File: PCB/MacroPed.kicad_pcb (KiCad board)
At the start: 2 copper layers, 82.4 x 52.1 mm, 11 parts, among them J1 Conn_01x02_Socket, J2 Conn_01x02_Socket, J3 Conn_01x02_Socket, J4 Conn_01x02_Socket, J5 Conn_01x02_Socket, J6 Conn_01x02_Socket, J7 Conn_01x02_Socket, J8 Conn_01x02_Socket, J9 Conn_01x02_Socket, SW1 SW_SPST, U1 Pico

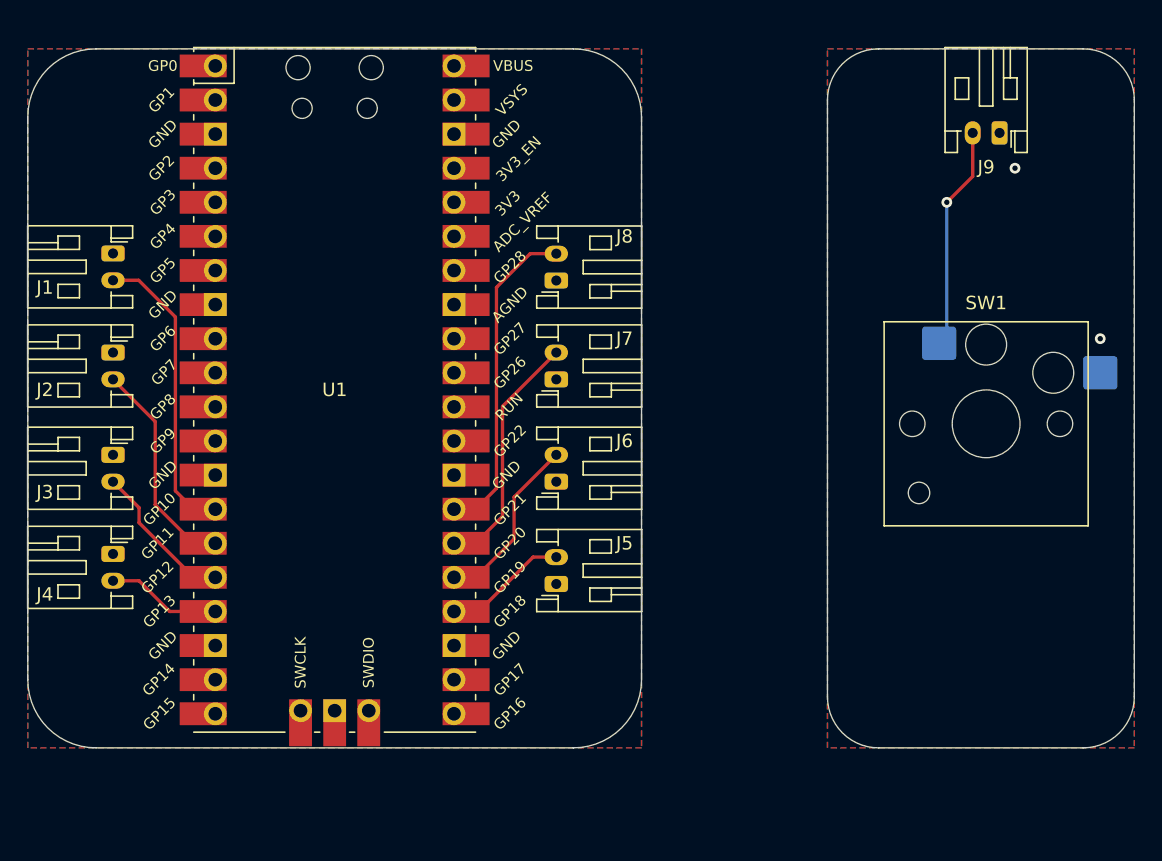
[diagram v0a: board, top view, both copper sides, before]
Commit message: Separated daughterboard to sub-project, added mounting holes
Signed-off-by: Devnol <pgkoutsoumanis@gmail.com>
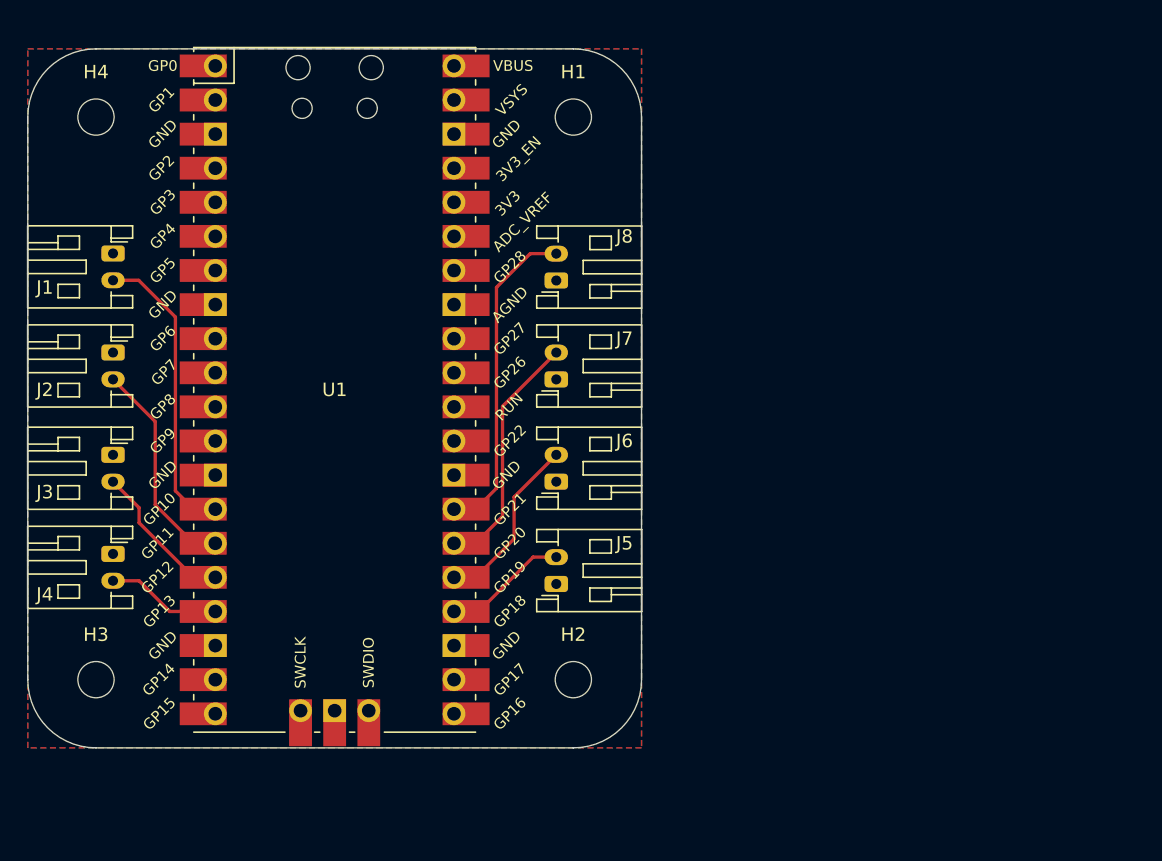
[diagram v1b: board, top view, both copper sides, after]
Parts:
- removed J9: Conn_01x02_Socket, Connector_JST:JST_PH_S2B-PH-K_1x02_P2.00mm_Horizontal
- removed SW1: SW_SPST, PCM_Switch_Keyboard_Hotswap_Kailh:SW_Hotswap_Kailh_Choc_V1V2_2.00u_90deg
- added H1: MountingHole, MountingHole:MountingHole_2.7mm_M2.5_DIN965, F.Cu at (82.5, 26.7)
- added H2: MountingHole, MountingHole:MountingHole_2.7mm_M2.5_DIN965, F.Cu at (82.5, 68.6)
- added H3: MountingHole, MountingHole:MountingHole_2.7mm_M2.5_DIN965, F.Cu at (47.0, 68.6)
- added H4: MountingHole, MountingHole:MountingHole_2.7mm_M2.5_DIN965, F.Cu at (47.0, 26.7)
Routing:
- net Net-(J9-Pin_2): track 16.7 -> 0.00 mm, vias 1 -> 0
- net /Foot Switch/GND: vias 2 -> 0
- removed copper zone on B.Cu, net /Foot Switch/GND
- removed copper zone on F.Cu, net /Foot Switch/GND
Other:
- board size 82.4 x 52.1 mm -> 45.7 x 52.1 mm

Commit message: Move connectors to one side, change dimensions to proper units
Signed-off-by: Devnol <pgkoutsoumanis@gmail.com>
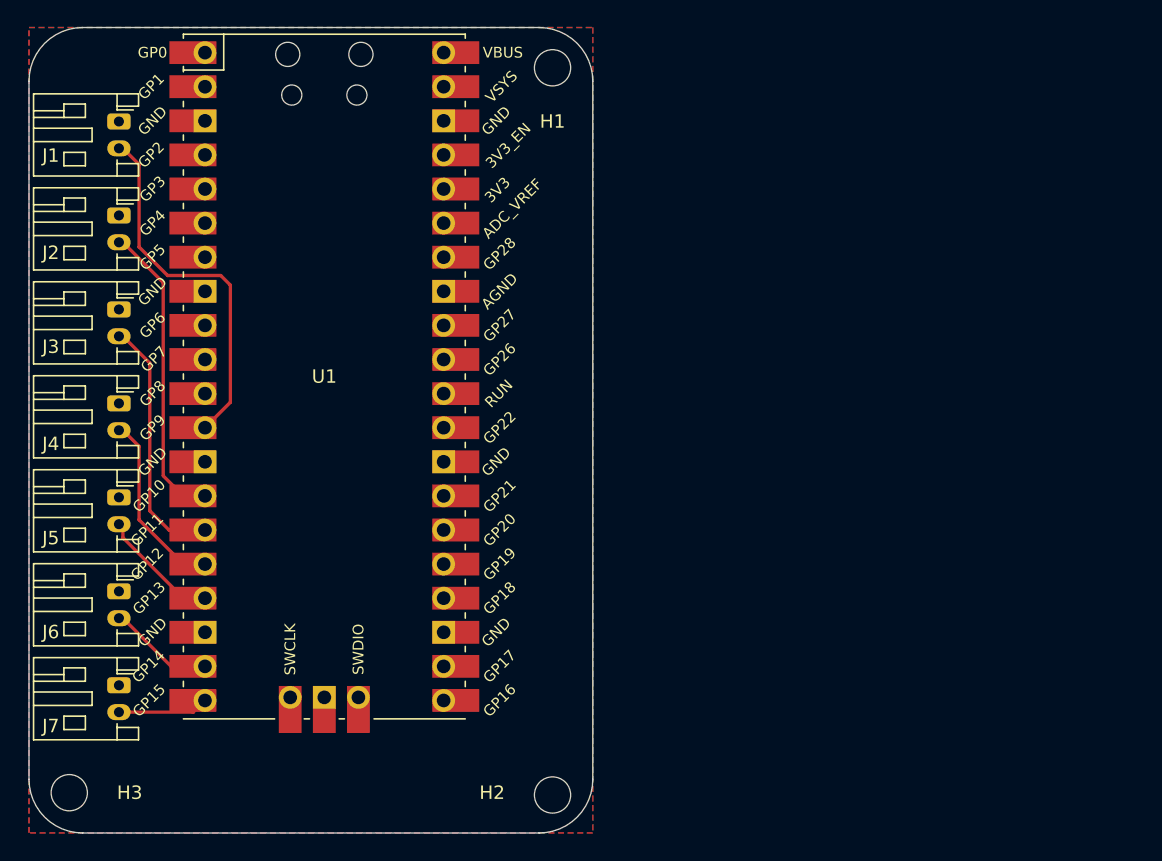
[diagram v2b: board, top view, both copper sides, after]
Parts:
- removed H4: MountingHole, MountingHole:MountingHole_2.7mm_M2.5_DIN965
- removed J8: Conn_01x02_Socket, Connector_JST:JST_PH_S2B-PH-K_1x02_P2.00mm_Horizontal
- moved J7 39.8 mm to (48.7, 69.0), turned to -90 degrees
- moved J6 33.6 mm to (48.7, 62.0), turned to -90 degrees
- moved J5 33.2 mm to (48.7, 55.0), turned to -90 degrees
- moved J4 11.2 mm to (48.7, 48.0)
- moved J3 10.8 mm to (48.7, 41.0)
- moved J2 10.2 mm to (48.7, 34.0)
- moved J1 9.84 mm to (48.7, 27.0)
- moved H2 8.73 mm to (81.0, 77.2)
- moved H3 8.65 mm to (45.0, 77.0)
- moved H1 3.98 mm to (81.0, 23.0)
- moved U1 1.25 mm to (64.0, 46.0)
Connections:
- U1 pad 12: unconnected-(U1-GPIO9-Pad12) -> Net-(J1-Pin_2)
- U1 pad 14: Net-(J1-Pin_2) -> Net-(J2-Pin_2)
- U1 pad 15: Net-(J2-Pin_2) -> Net-(J3-Pin_2)
- U1 pad 16: Net-(J3-Pin_2) -> Net-(J4-Pin_2)
- U1 pad 17: Net-(J4-Pin_2) -> Net-(J5-Pin_2)
- U1 pad 19: unconnected-(U1-GPIO14-Pad19) -> Net-(J6-Pin_2)
- U1 pad 20: unconnected-(U1-GPIO15-Pad20) -> Net-(J7-Pin_2)
- U1 pad 24: Net-(J5-Pin_2) -> unconnected-(U1-GPIO18-Pad24)
- U1 pad 25: Net-(J6-Pin_2) -> unconnected-(U1-GPIO19-Pad25)
- U1 pad 26: Net-(J7-Pin_2) -> unconnected-(U1-GPIO20-Pad26)
- U1 pad 27: Net-(J8-Pin_2) -> unconnected-(U1-GPIO21-Pad27)
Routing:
- net Net-(J8-Pin_2): track 24.3 -> 0.00 mm
- net Net-(J7-Pin_2): track 18.3 -> 6.47 mm
- net Net-(J3-Pin_2): track 11.2 -> 18.5 mm
- net Net-(J2-Pin_2): track 16.3 -> 22.4 mm
- net Net-(J6-Pin_2): track 13.2 -> 7.60 mm
- net Net-(J1-Pin_2): track 22.3 -> 27.2 mm
- net Net-(J4-Pin_2): track 8.57 -> 13.4 mm
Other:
- board size 45.7 x 52.1 mm -> 42 x 60 mm

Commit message: Change board dimensions to real units
Signed-off-by: Devnol <pgkoutsoumanis@gmail.com>
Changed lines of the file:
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@@
     (fp_line (start 3.95 6.25) (end 3.95 -1.35)
       (stroke (width 0.1) (type solid)) (layer "F.Fab"))
-    (pad "1" thru_hole roundrect (at 0 0 270) (size 1.2 1.75) (drill 0.75) (layers "*.Cu" "*.Mask") (roundrect_rratio 0.208333)
+    (pad "1" thru_hole roundrect (at 0 0 270) (size 1.2 1.75) (drill 0.75) (layers "*.Cu" "*.Mask") (roundrect_rratio 0.2083333333)
       (net 10 "/GND") (pinfunction "Pin_1") (pintype "passive"))
     (pad "2" thru_hole oval (at 2 0 270) (size 1.2 1.75) (drill 0.75) (layers "*.Cu" "*.Mask")
@@
     (fp_line (start 3.95 6.25) (end 3.95 -1.35)
       (stroke (width 0.1) (type solid)) (layer "F.Fab"))
-    (pad "1" thru_hole roundrect (at 0 0 270) (size 1.2 1.75) (drill 0.75) (layers "*.Cu" "*.Mask") (roundrect_rratio 0.208333)
+    (pad "1" thru_hole roundrect (at 0 0 270) (size 1.2 1.75) (drill 0.75) (layers "*.Cu" "*.Mask") (roundrect_rratio 0.2083333333)
       (net 10 "/GND") (pinfunction "Pin_1") (pintype "passive"))
     (pad "2" thru_hole oval (at 2 0 270) (size 1.2 1.75) (drill 0.75) (layers "*.Cu" "*.Mask")
@@
     (fp_line (start 3.95 6.25) (end 3.95 -1.35)
       (stroke (width 0.1) (type solid)) (layer "F.Fab"))
-    (pad "1" thru_hole roundrect (at 0 0 270) (size 1.2 1.75) (drill 0.75) (layers "*.Cu" "*.Mask") (roundrect_rratio 0.208333)
+    (pad "1" thru_hole roundrect (at 0 0 270) (size 1.2 1.75) (drill 0.75) (layers "*.Cu" "*.Mask") (roundrect_rratio 0.2083333333)
       (net 10 "/GND") (pinfunction "Pin_1") (pintype "passive"))
     (pad "2" thru_hole oval (at 2 0 270) (size 1.2 1.75) (drill 0.75) (layers "*.Cu" "*.Mask")
@@
     (fp_line (start 3.95 6.25) (end 3.95 -1.35)
       (stroke (width 0.1) (type solid)) (layer "F.Fab"))
-    (pad "1" thru_hole roundrect (at 0 0 270) (size 1.2 1.75) (drill 0.75) (layers "*.Cu" "*.Mask") (roundrect_rratio 0.208333)
+    (pad "1" thru_hole roundrect (at 0 0 270) (size 1.2 1.75) (drill 0.75) (layers "*.Cu" "*.Mask") (roundrect_rratio 0.2083333333)
       (net 10 "/GND") (pinfunction "Pin_1") (pintype "passive"))
     (pad "2" thru_hole oval (at 2 0 270) (size 1.2 1.75) (drill 0.75) (layers "*.Cu" "*.Mask")
@@
     (fp_line (start 3.95 6.25) (end 3.95 -1.35)
       (stroke (width 0.1) (type solid)) (layer "F.Fab"))
-    (pad "1" thru_hole roundrect (at 0 0 270) (size 1.2 1.75) (drill 0.75) (layers "*.Cu" "*.Mask") (roundrect_rratio 0.208333)
+    (pad "1" thru_hole roundrect (at 0 0 270) (size 1.2 1.75) (drill 0.75) (layers "*.Cu" "*.Mask") (roundrect_rratio 0.2083333333)
       (net 10 "/GND") (pinfunction "Pin_1") (pintype "passive"))
     (pad "2" thru_hole oval (at 2 0 270) (size 1.2 1.75) (drill 0.75) (layers "*.Cu" "*.Mask")
@@
     (fp_line (start 3.95 6.25) (end 3.95 -1.35)
       (stroke (width 0.1) (type solid)) (layer "F.Fab"))
-    (pad "1" thru_hole roundrect (at 0 0 270) (size 1.2 1.75) (drill 0.75) (layers "*.Cu" "*.Mask") (roundrect_rratio 0.208333)
+    (pad "1" thru_hole roundrect (at 0 0 270) (size 1.2 1.75) (drill 0.75) (layers "*.Cu" "*.Mask") (roundrect_rratio 0.2083333333)
       (net 10 "/GND") (pinfunction "Pin_1") (pintype "passive"))
     (pad "2" thru_hole oval (at 2 0 270) (size 1.2 1.75) (drill 0.75) (layers "*.Cu" "*.Mask")
@@
     (fp_line (start 3.95 6.25) (end 3.95 -1.35)
       (stroke (width 0.1) (type solid)) (layer "F.Fab"))
-    (pad "1" thru_hole roundrect (at 0 0 270) (size 1.2 1.75) (drill 0.75) (layers "*.Cu" "*.Mask") (roundrect_rratio 0.208333)
+    (pad "1" thru_hole roundrect (at 0 0 270) (size 1.2 1.75) (drill 0.75) (layers "*.Cu" "*.Mask") (roundrect_rratio 0.2083333333)
       (net 10 "/GND") (pinfunction "Pin_1") (pintype "passive"))
     (pad "2" thru_hole oval (at 2 0 270) (size 1.2 1.75) (drill 0.75) (layers "*.Cu" "*.Mask")

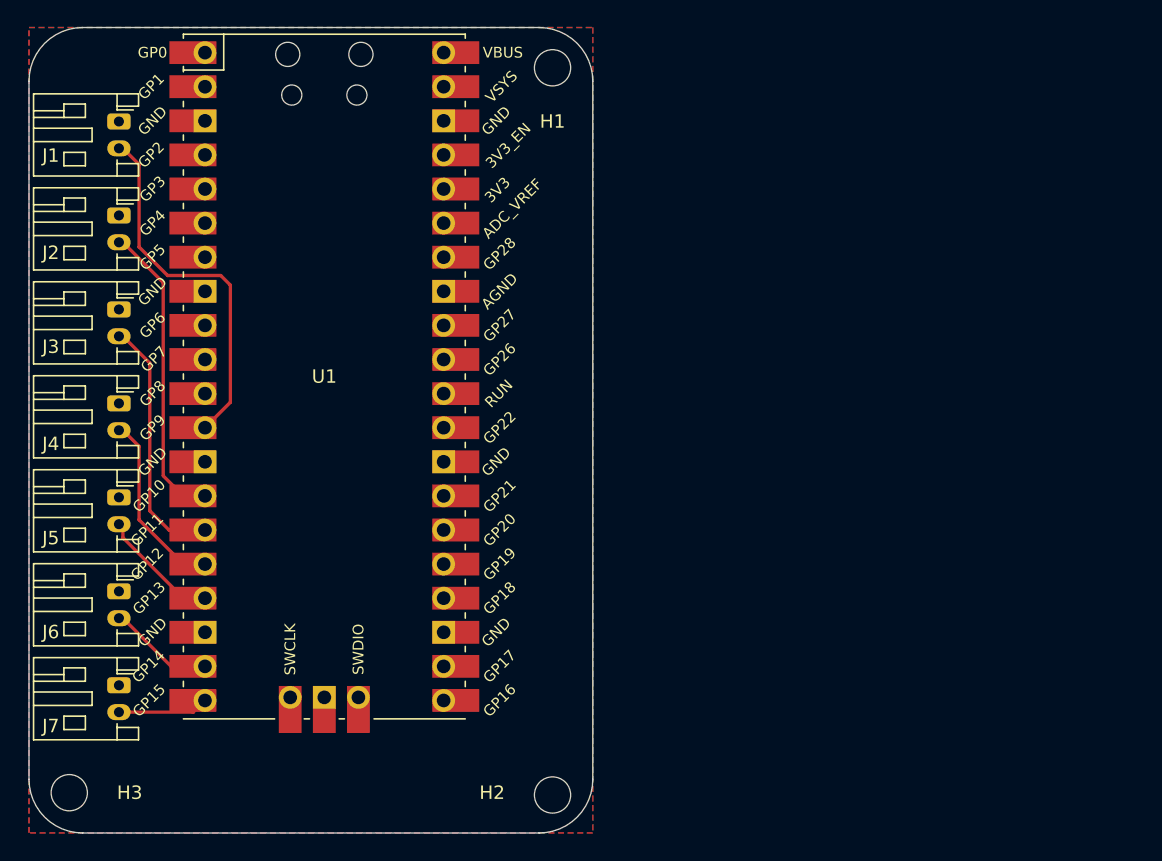
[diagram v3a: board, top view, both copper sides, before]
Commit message: Moved JST connector to edge of footboard
Signed-off-by: Devnol <pgkoutsoumanis@gmail.com>
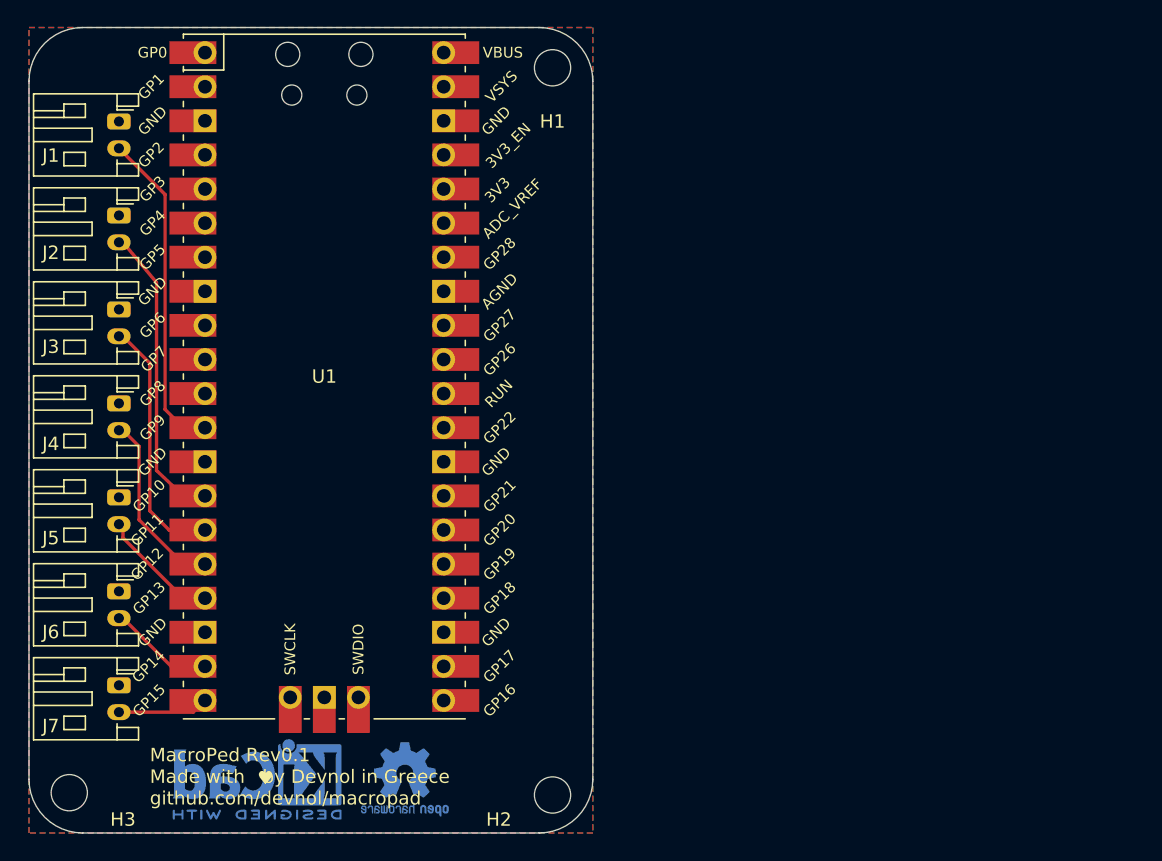
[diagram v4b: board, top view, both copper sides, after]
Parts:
- added Logo1: OSHW-Logo2_7.3x6mm_Copper, Symbol:OSHW-Logo2_7.3x6mm_Copper, B.Cu at (70.0, 76.0)
- added Logo2: KiCad-Logo2_5mm_Copper, Symbol:KiCad-Logo2_5mm_Copper, B.Cu at (59.0, 76.0)
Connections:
- U1 pad 38: unconnected-(U1-GND-Pad38) -> /GND
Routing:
- net Net-(J1-Pin_2): track 27.2 -> 24.4 mm
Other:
- board text added: "MacroPed Rev0.1 Made with ︎ by Devnol in Greece github.com/devnol/macropad"
- board text added: "♥︎"

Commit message: Shorten main board
Signed-off-by: Devnol <pgkoutsoumanis@gmail.com>
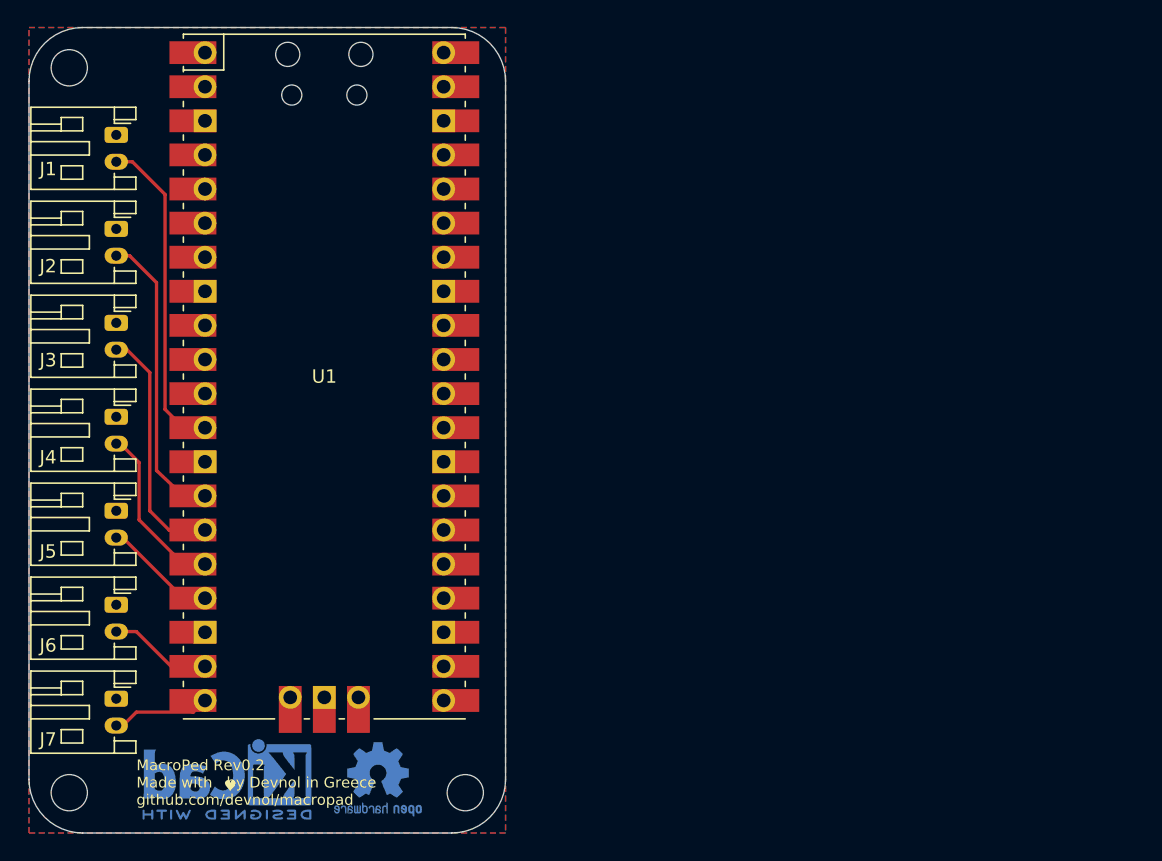
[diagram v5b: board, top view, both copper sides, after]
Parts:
- moved H2 36.0 mm to (45.0, 77.0)
- moved H1 36.0 mm to (45.0, 23.0)
- moved H3 29.5 mm to (74.5, 77.0)
- moved Logo2 2.25 mm to (56.8, 76.0)
- moved Logo1 2.00 mm to (68.0, 76.0)
- moved J1 1.02 mm to (48.5, 28.0)
- moved J2 1.02 mm to (48.5, 35.0)
- moved J3 1.02 mm to (48.5, 42.0)
- moved J4 1.02 mm to (48.5, 49.0)
- moved J5 1.02 mm to (48.5, 56.0)
- moved J6 1.02 mm to (48.5, 63.0)
- moved J7 1.02 mm to (48.5, 70.0)
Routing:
- net Net-(J4-Pin_2): track 13.4 -> 12.5 mm
- net Net-(J5-Pin_2): track 8.98 -> 8.18 mm
- net Net-(J3-Pin_2): track 18.5 -> 17.9 mm
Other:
- board size 42 x 60 mm -> 35.5 x 60 mm
- board text added: "MacroPed Rev0.2 Made with ︎ by Devnol in Greece github.com/devnol/macropad"
- board text removed: "MacroPed Rev0.1 Made with ︎ by Devnol in Greece github.com/devnol/macropad"
